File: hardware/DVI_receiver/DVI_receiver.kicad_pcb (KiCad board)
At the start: 4 copper layers, 43 x 25.8 mm, 59 parts, among them J1 HDMI_A, J2 Conn_01x05_Pin, J6 DF12NB(3.0)-30DS-0.5V(51), J7 DF12NB(3.0)-30DS-0.5V(51), Q1 BSS138, U1 TXS0102DCUR, U5 AMS1117-3.3, U8 TFP401

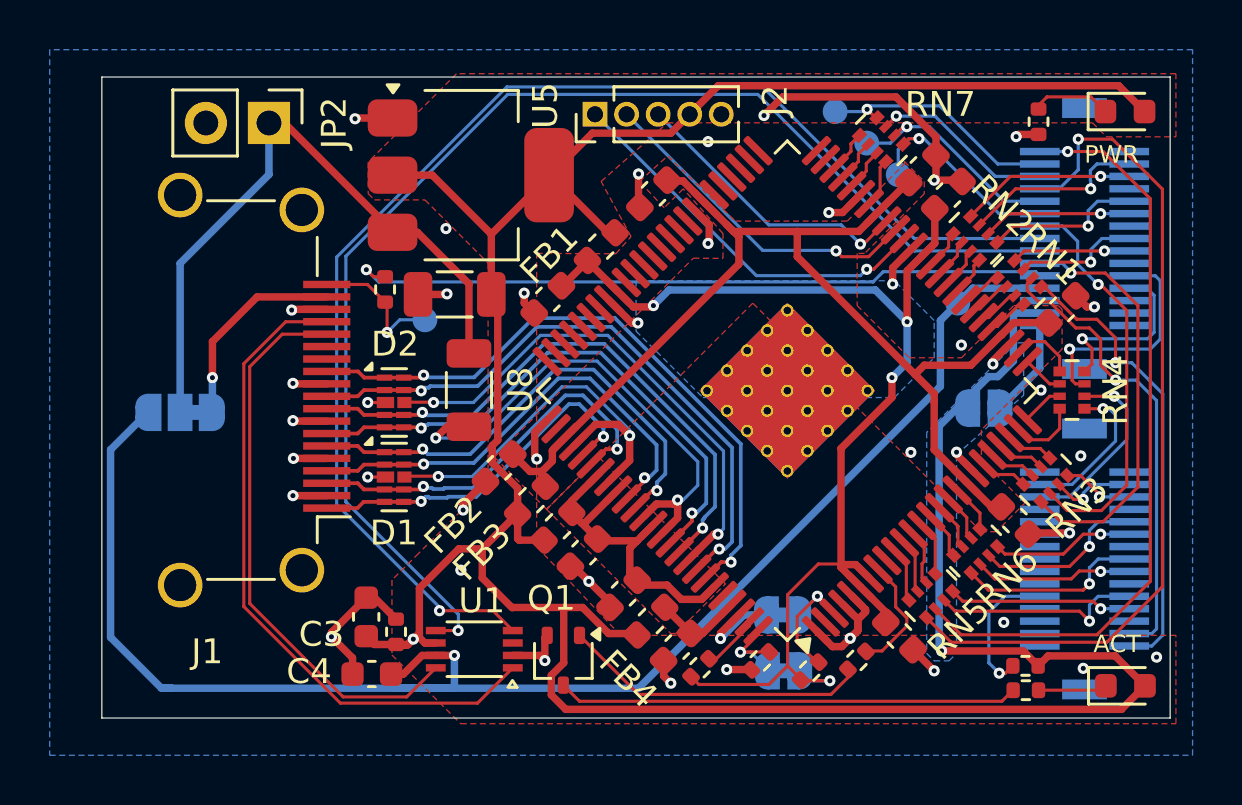
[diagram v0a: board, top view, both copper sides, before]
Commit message: correction of DRC constraints to allow 4-layer boards pass DFM
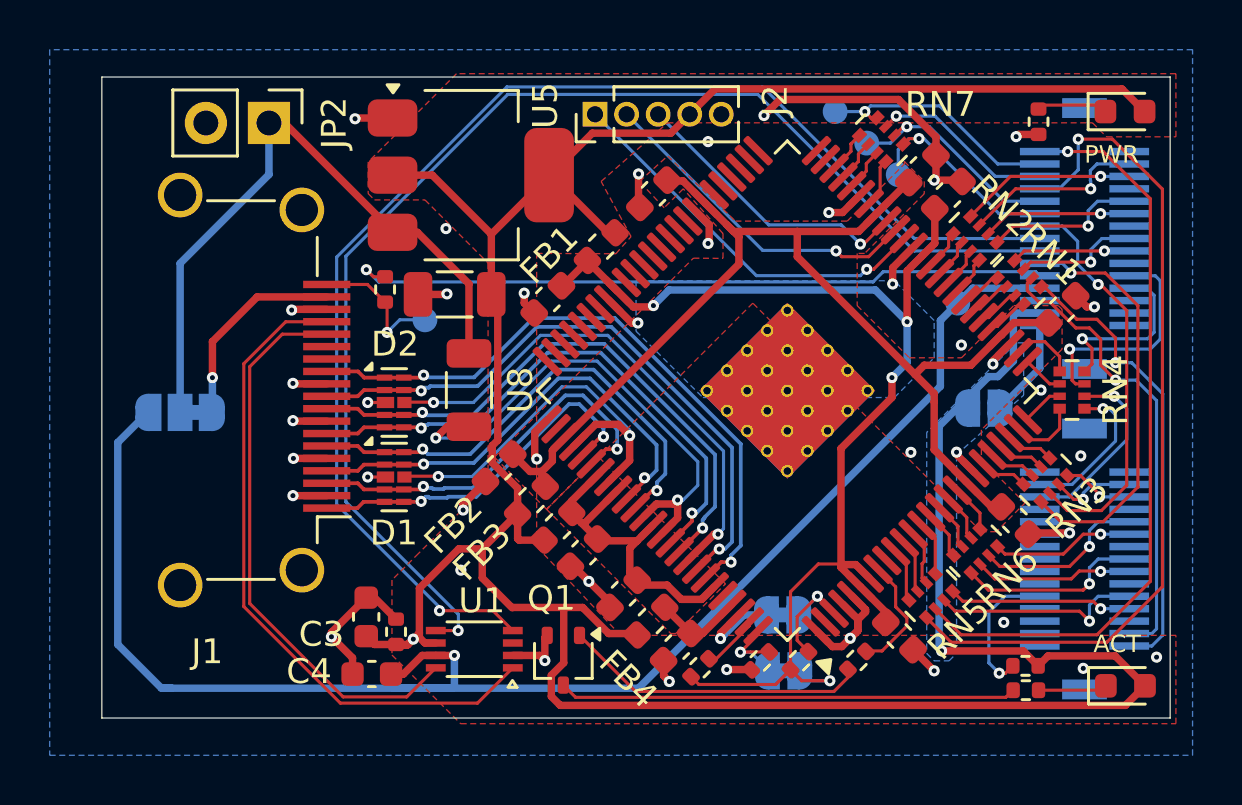
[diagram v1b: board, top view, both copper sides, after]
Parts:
- moved R13 0.59 mm to (137.5, 105.0)
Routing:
- net /fpga/ST: track 5.39 -> 4.77 mm
